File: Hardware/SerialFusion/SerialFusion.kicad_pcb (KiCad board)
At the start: 2 copper layers, 58 parts, among them J1 USB Type C, J2 ESP32_Prog, J3 UART_Debug, J4 120E_Sel, J5 RS232, J6 RS485, Q1 MMBT3904, Q2 MMBT3904, Q3 MMBT3904, SW1 EN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

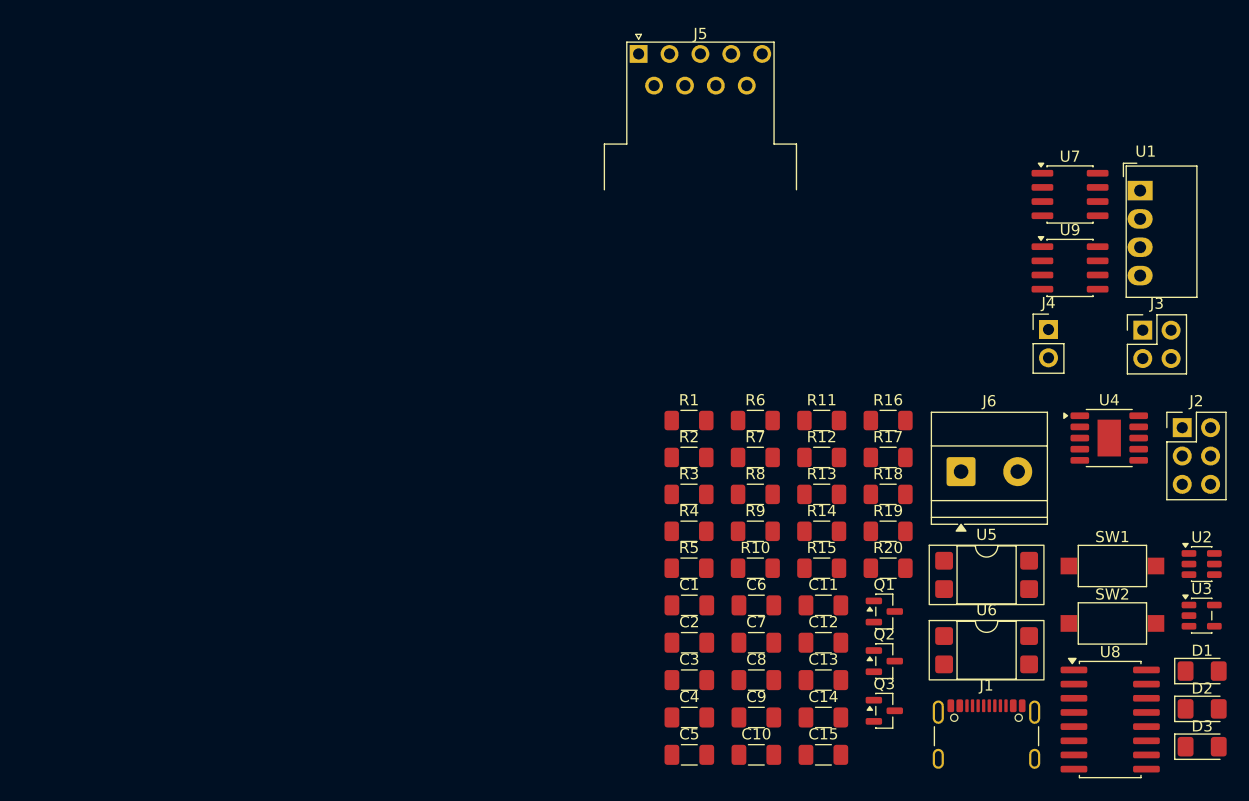
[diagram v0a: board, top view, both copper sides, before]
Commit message: First stage design for Rev A is completed & files updated
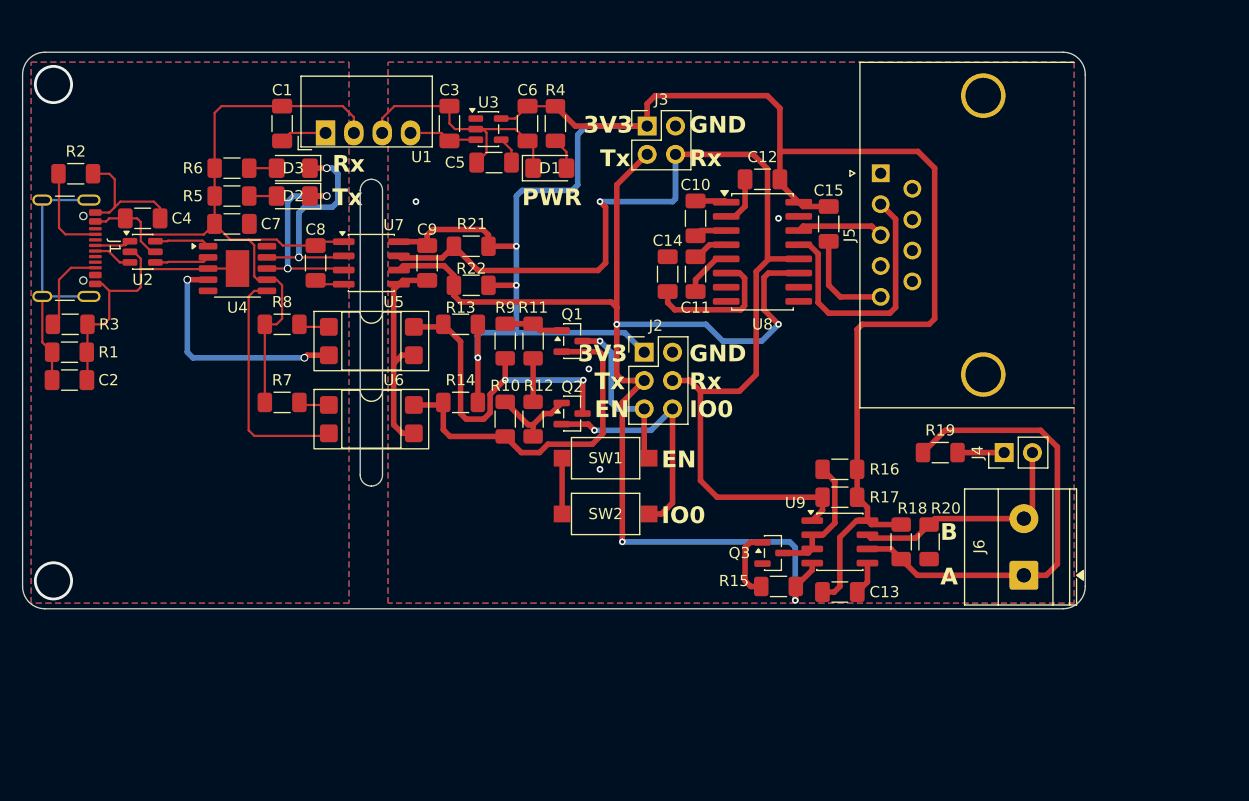
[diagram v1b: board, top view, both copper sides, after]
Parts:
- added R21: 4K7, Resistor_SMD:R_1206_3216Metric_Pad1.30x1.75mm_HandSolder, F.Cu at (82.0, 82.5)
- added R22: 4K7, Resistor_SMD:R_1206_3216Metric_Pad1.30x1.75mm_HandSolder, F.Cu at (82.0, 86.0)
- J5: footprint Connector_Dsub:DSUB-9_Pins_Horizontal_P2.77x2.84mm_EdgePinOffset9.40mm -> Connector_Dsub:DSUB-9_Socket_Horizontal_P2.77x2.84mm_EdgePinOffset14.56mm_Housed_MountingHolesOffset8.20mm
- moved U2 99.0 mm to (52.5, 83.0)
- moved D3 96.6 mm to (66.0, 75.5), turned to 180 degrees
- moved J1 94.8 mm to (44.6, 82.7), turned to -90 degrees
- moved D2 93.6 mm to (66.0, 78.0), turned to 180 degrees
- moved U4 79.6 mm to (61.0, 84.5)
- moved U3 77.4 mm to (83.5, 72.0)
- moved D1 73.8 mm to (89.0, 75.5)
- moved U1 73.2 mm to (68.9, 72.3), turned to 90 degrees
- moved C4 66.4 mm to (52.5, 80.0)
- moved U7 62.9 mm to (73.0, 84.0)
- moved R2 60.6 mm to (46.5, 76.0)
- moved C2 60.3 mm to (45.9, 94.5)
- moved C7 60.2 mm to (60.5, 80.5)
- moved U5 59.0 mm to (73.0, 91.0)
- moved U6 58.9 mm to (73.0, 98.0)
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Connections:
- U3 pad 3: GND1 -> +5VA
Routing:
- net +3.3V: track 0.00 -> 175.8 mm, vias 0 -> 3
- net Tx: track 0.00 -> 110.3 mm, vias 0 -> 4
- net Rx: track 0.00 -> 97.8 mm, vias 0 -> 1
- net +5V: track 0.00 -> 69.9 mm
- net GND1: track 0.00 -> 63.8 mm, vias 0 -> 4
- net GND: track 0.00 -> 45.6 mm, vias 0 -> 2
- net Net-(J6-Pin_1): track 0.00 -> 42.4 mm
- net RTS: track 0.00 -> 31.9 mm
- net DTR: track 0.00 -> 30.0 mm, vias 0 -> 2
- net Net-(J1-SHIELD): track 0.00 -> 24.9 mm
- net Net-(U8-R1IN): track 0.00 -> 23.8 mm
- net IO0: track 0.00 -> 21.9 mm, vias 0 -> 1
- net Net-(U4-~{DTR}): track 0.00 -> 21.4 mm, vias 0 -> 2
- net Net-(U4-~{RTS}): track 0.00 -> 21.3 mm
- net Net-(J4-Pin_2): track 0.00 -> 21.1 mm
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- added copper zone on B.Cu, net GND
- added copper zone on F.Cu, net GND
- added copper zone on B.Cu, net GND1
- added copper zone on F.Cu, net GND1
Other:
- board outline added: 95.3 x 49.9 mm
- board text added: "3V3"
- board text added: "A"
- board text added: "B"
- board text added: "EN"
- board text added: "GND"
- board text added: "IO0"
- board text added: "PWR"
- board text added: "Rx"
- board text added: "Tx"
